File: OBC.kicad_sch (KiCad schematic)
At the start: 0 parts

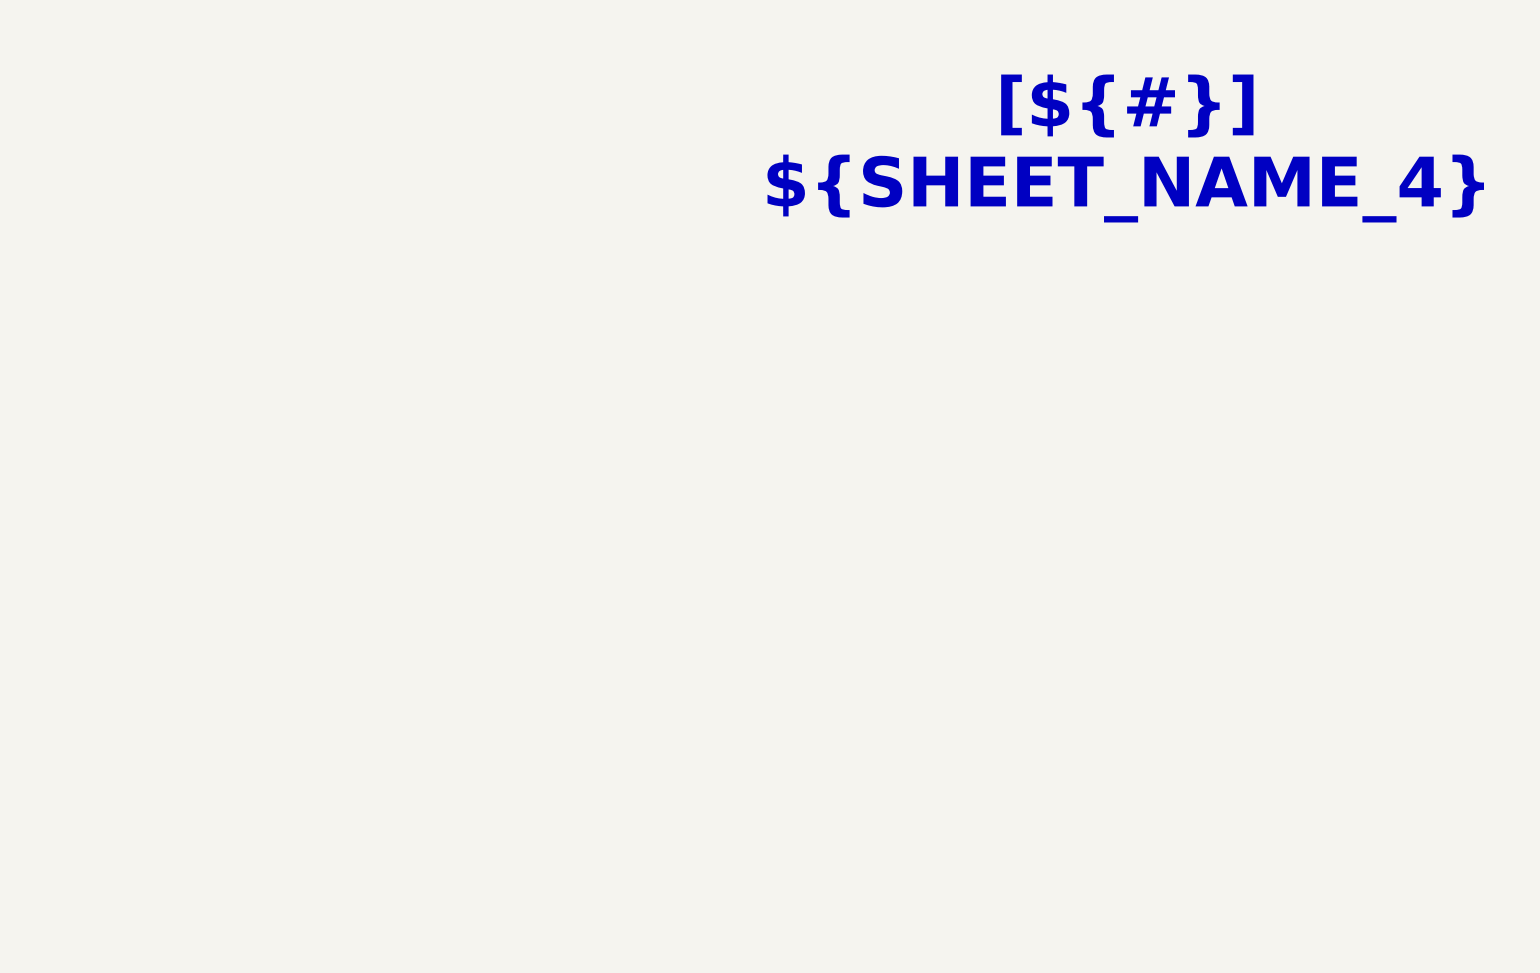
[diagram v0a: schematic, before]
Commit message: Pasted schematics from previous design
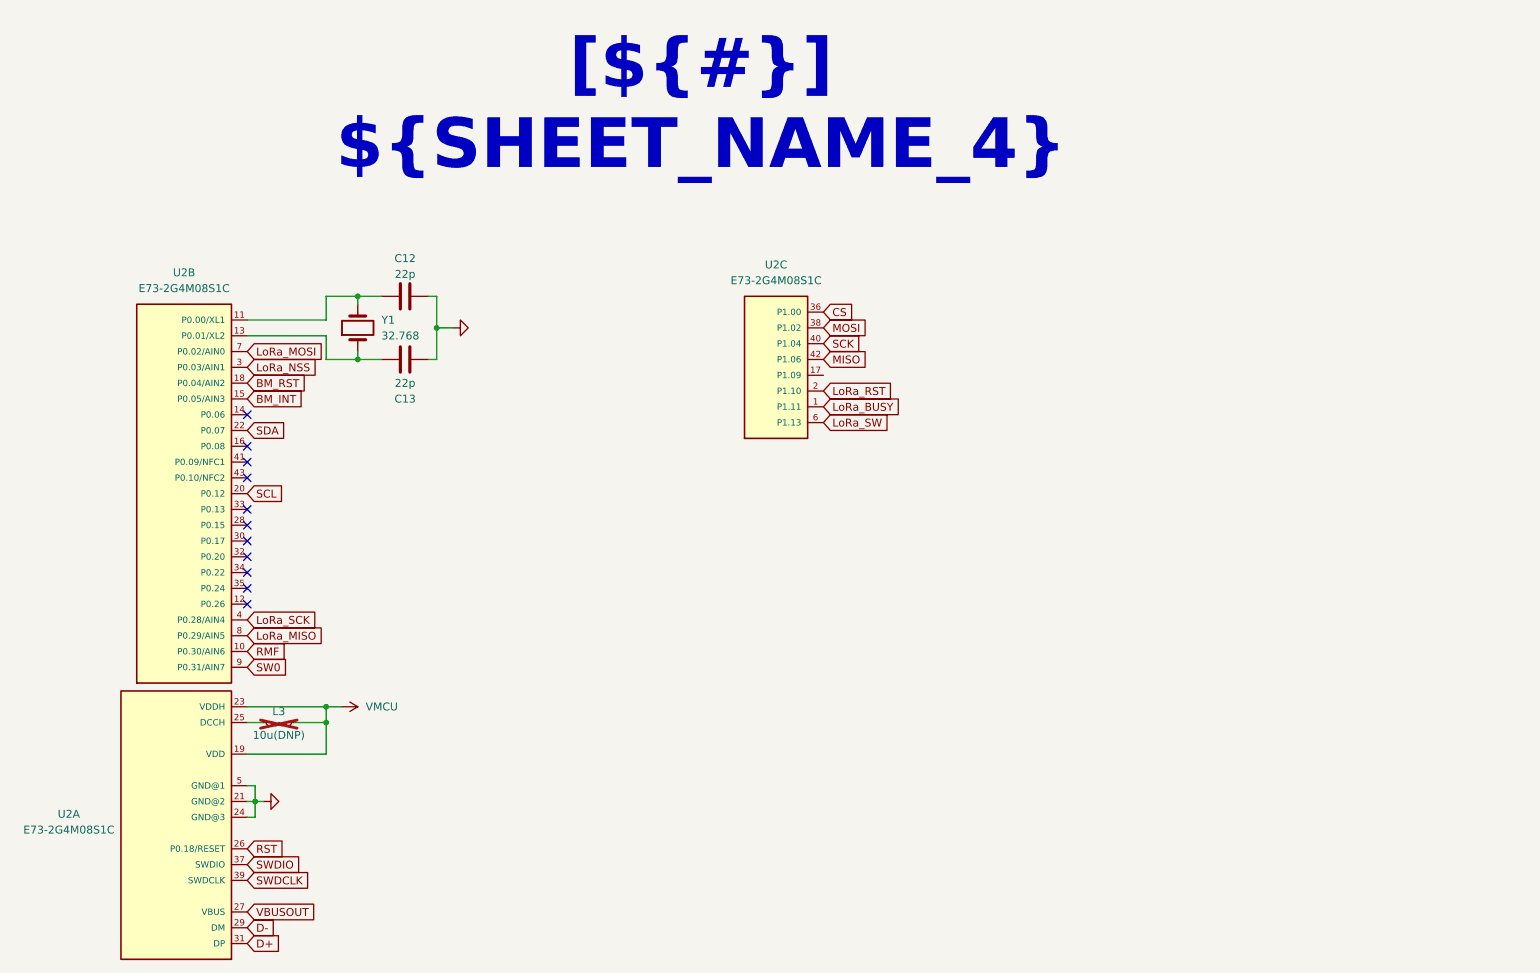
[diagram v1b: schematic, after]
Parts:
- added C12, C13: 22p, Capacitor_SMD:C_1206_3216Metric_Pad1.33x1.80mm_HandSolder, symbol Device:C
- added L3: 10u(DNP), Inductor_SMD:L_Changjiang_FTC201610D, symbol Device:L_Small
- added U2: E73-2G4M08S1C, Project_Components:E73-2G4M08S1C, symbol Project_Components:E73-2G4M08S1C
- added Y1: 32.768, Project_Components:WE-XTAL_CFPX-217, symbol Device:Crystal
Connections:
- new net: C12.2, U2.11 (P0.00/XL1), Y1.2
- new net: C13.2, U2.13 (P0.01/XL2), Y1.1
- new net: L3.1, U2.25 (DCCH)
- new net BM_INT: U2.15 (P0.05/AIN3)
- new net BM_RST: U2.18 (P0.04/AIN2)
- new net CS: U2.36 (P1.00)
- new net D+: U2.31 (DP)
- new net D-: U2.29 (DM)
- new net GND: C12.1, C13.1, U2.21 (GND@2), U2.24 (GND@3), U2.5 (GND@1)
- new net LoRa_BUSY: U2.1 (P1.11)
- new net LoRa_MISO: U2.8 (P0.29/AIN5)
- new net LoRa_MOSI: U2.7 (P0.02/AIN0)
- new net LoRa_NSS: U2.3 (P0.03/AIN1)
- new net LoRa_RST: U2.2 (P1.10)
- new net LoRa_SCK: U2.4 (P0.28/AIN4)
- new net LoRa_SW: U2.6 (P1.13)
- new net MISO: U2.42 (P1.06)
- new net MOSI: U2.38 (P1.02)
- new net RMF: U2.10 (P0.30/AIN6)
- new net RST: U2.26 (P0.18/RESET)
- new net SCK: U2.40 (P1.04)
- new net SCL: U2.20 (P0.12)
- new net SDA: U2.22 (P0.07)
- new net SW0: U2.9 (P0.31/AIN7)
- new net SWDCLK: U2.39 (SWDCLK)
- new net SWDIO: U2.37 (SWDIO)
- new net VBUSOUT: U2.27 (VBUS)
- new net VMCU: L3.2, U2.19 (VDD), U2.23 (VDDH)
- no-connect marks 0 -> 11

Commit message: Changed a few preferences
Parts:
- C12, C13: footprint Capacitor_SMD:C_1206_3216Metric_Pad1.33x1.80mm_HandSolder -> Capacitor_SMD:C_0603_1608Metric
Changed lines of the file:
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@@
 			)
 		)
-		(property "Footprint" "Capacitor_SMD:C_1206_3216Metric_Pad1.33x1.80mm_HandSolder"
+		(property "Footprint" "Capacitor_SMD:C_0603_1608Metric"
 			(at 90.17 67.6148 0)
 			(hide yes)
@@
 			)
 		)
-		(property "Footprint" "Capacitor_SMD:C_1206_3216Metric_Pad1.33x1.80mm_HandSolder"
+		(property "Footprint" "Capacitor_SMD:C_0603_1608Metric"
 			(at 90.17 59.3852 0)
 			(hide yes)

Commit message: Finished preliminary project schematics and architecture
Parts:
- U1: renamed from U2; footprint Project_Components:E73-2G4M08S1C -> E73-2G4M08S1C:E73-2G4M08S1C
- renumbered C12 to C1, C13 to C2, L3 to L1

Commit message: Edited ci.yaml
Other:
- moved on the sheet: C1, C2, Y1
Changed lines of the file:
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@@
-	)
-	(junction
-		(at 86.36 68.58)
-		(diameter 0)
-		(color 0 0 0 0)
 	)
 	(junction
@@
 	)
 	(junction
-		(at 99.06 63.5)
+		(at 88.9 68.58)
 		(diameter 0)
 		(color 0 0 0 0)
 	)
 	(junction
-		(at 86.36 58.42)
+		(at 101.6 63.5)
 		(diameter 0)
 		(color 0 0 0 0)
@@
 		(color 0 0 0 0)
 	)
+	(junction
+		(at 88.9 58.42)
+		(diameter 0)
+		(color 0 0 0 0)
+	)
 	(no_connect
 		(at 68.58 92.71)
@@
 	(wire
 		(pts
-			(xy 81.28 62.23) (xy 68.58 62.23)
+			(xy 82.55 62.23) (xy 68.58 62.23)
 		)
 		(stroke
@@
 	(wire
 		(pts
-			(xy 99.06 63.5) (xy 99.06 58.42)
-		)
-		(stroke
-			(width 0)
-			(type default)
-		)
-	)
-	(wire
-		(pts
-			(xy 81.28 68.58) (xy 81.28 64.77)
+			(xy 101.6 63.5) (xy 101.6 58.42)
+		)
+		(stroke
+			(width 0)
+			(type default)
+		)
+	)
+	(wire
+		(pts
+			(xy 82.55 68.58) (xy 82.55 64.77)
 		)
 		(stroke
@@
 	(wire
 		(pts
-			(xy 81.28 68.58) (xy 86.36 68.58)
-		)
-		(stroke
-			(width 0)
-			(type default)
-		)
-	)
-	(wire
-		(pts
-			(xy 86.36 58.42) (xy 86.36 59.69)
+			(xy 82.55 68.58) (xy 88.9 68.58)
+		)
+		(stroke
+			(width 0)
+			(type default)
+		)
+	)
+	(wire
+		(pts
+			(xy 88.9 58.42) (xy 88.9 59.69)
 		)
 		(stroke
@@
 	(wire
 		(pts
-			(xy 81.28 58.42) (xy 81.28 62.23)
-		)
-		(stroke
-			(width 0)
-			(type default)
-		)
-	)
-	(wire
-		(pts
-			(xy 101.6 63.5) (xy 99.06 63.5)
+			(xy 82.55 58.42) (xy 82.55 62.23)
+		)
+		(stroke
+			(width 0)
+			(type default)
+		)
+	)
+	(wire
+		(pts
+			(xy 104.14 63.5) (xy 101.6 63.5)
 		)
 		(stroke
@@
 	(wire
 		(pts
-			(xy 81.28 64.77) (xy 68.58 64.77)
+			(xy 82.55 64.77) (xy 68.58 64.77)
 		)
 		(stroke
@@
 	(wire
 		(pts
-			(xy 99.06 58.42) (xy 97.79 58.42)
+			(xy 101.6 58.42) (xy 100.33 58.42)
 		)
 		(stroke
@@
 	(wire
 		(pts
-			(xy 86.36 68.58) (xy 90.17 68.58)
+			(xy 88.9 68.58) (xy 92.71 68.58)
 		)
 		(stroke
@@
 	(wire
 		(pts
-			(xy 86.36 68.58) (xy 86.36 67.31)
+			(xy 88.9 68.58) (xy 88.9 67.31)
 		)
 		(stroke
@@
 	(wire
 		(pts
-			(xy 86.36 58.42) (xy 90.17 58.42)
+			(xy 88.9 58.42) (xy 92.71 58.42)
 		)
 		(stroke
@@
 	(wire
 		(pts
-			(xy 97.79 68.58) (xy 99.06 68.58)
+			(xy 100.33 68.58) (xy 101.6 68.58)
 		)
 		(stroke
@@
 	(wire
 		(pts
-			(xy 81.28 58.42) (xy 86.36 58.42)
+			(xy 82.55 58.42) (xy 88.9 58.42)
 		)
 		(stroke
@@
 	(wire
 		(pts
-			(xy 99.06 68.58) (xy 99.06 63.5)
+			(xy 101.6 68.58) (xy 101.6 63.5)
 		)
 		(stroke
@@
 	(symbol
 		(lib_id "power:GND")
-		(at 101.6 63.5 90)
+		(at 104.14 63.5 90)
 		(unit 1)
 		(body_style 1)
@@
 		(fields_autoplaced yes)
 		(property "Reference" "#PWR041"
-			(at 107.95 63.5 0)
+			(at 110.49 63.5 0)
 			(hide yes)
 			(show_name no)
@@
 		)
 		(property "Value" "GND"
-			(at 105.41 63.4999 90)
+			(at 107.95 63.4999 90)
 			(hide yes)
 			(show_name no)
@@
 		)
 		(property "Footprint" ""
-			(at 101.6 63.5 0)
+			(at 104.14 63.5 0)
 			(hide yes)
 			(show_name no)
@@
 		)
 		(property "Datasheet" ""
-			(at 101.6 63.5 0)
+			(at 104.14 63.5 0)
 			(hide yes)
 			(show_name no)
@@
 		)
 		(property "Description" "Power symbol creates a global label with name \"GND\" , ground"
-			(at 101.6 63.5 0)
+			(at 104.14 63.5 0)
 			(hide yes)
 			(show_name no)
@@
 	(symbol
 		(lib_id "Device:C")
-		(at 93.98 68.58 270)
+		(at 96.52 68.58 270)
 		(mirror x)
 		(unit 1)
@@
 		(dnp no)
 		(property "Reference" "C2"
-			(at 93.98 74.93 90)
+			(at 96.52 74.93 90)
 			(show_name no)
 			(do_not_autoplace no)
@@
 		)
 		(property "Value" "22p"
-			(at 93.98 72.39 90)
+			(at 96.52 72.39 90)
 			(show_name no)
 			(do_not_autoplace no)
@@
 		)
 		(property "Footprint" "Capacitor_SMD:C_0603_1608Metric"
-			(at 90.17 67.6148 0)
+			(at 92.71 67.6148 0)
 			(hide yes)
 			(show_name no)
@@
 		)
 		(property "Datasheet" ""
-			(at 93.98 68.58 0)
+			(at 96.52 68.58 0)
 			(hide yes)
 			(show_name no)
@@
 		)
 		(property "Description" "Unpolarized capacitor"
-			(at 93.98 68.58 0)
+			(at 96.52 68.58 0)
 			(hide yes)
 			(show_name no)
@@
 	(symbol
 		(lib_id "Device:Crystal")
-		(at 86.36 63.5 90)
+		(at 88.9 63.5 90)
 		(unit 1)
 		(body_style 1)
@@
 		(fields_autoplaced yes)
 		(property "Reference" "Y1"
-			(at 90.17 62.2299 90)
+			(at 92.71 62.2299 90)
 			(show_name no)
 			(do_not_autoplace no)
@@
 		)
 		(property "Value" "32.768"
-			(at 90.17 64.7699 90)
+			(at 92.71 64.7699 90)
 			(show_name no)
 			(do_not_autoplace no)
@@
 		)
 		(property "Footprint" "Project_Components:WE-XTAL_CFPX-217"
-			(at 86.36 63.5 0)
+			(at 88.9 63.5 0)
 			(hide yes)
 			(show_name no)
@@
 		)
 		(property "Datasheet" ""
-			(at 86.36 63.5 0)
+			(at 88.9 63.5 0)
 			(hide yes)
 			(show_name no)
@@
 		)
 		(property "Description" "Two pin crystal"
-			(at 86.36 63.5 0)
+			(at 88.9 63.5 0)
 			(hide yes)
 			(show_name no)
@@
 	(symbol
 		(lib_id "Device:C")
-		(at 93.98 58.42 270)
+		(at 96.52 58.42 270)
 		(unit 1)
 		(body_style 1)
@@
 		(dnp no)
 		(property "Reference" "C1"
-			(at 93.98 52.324 90)
+			(at 96.52 52.324 90)
 			(show_name no)
 			(do_not_autoplace no)
@@
 		)
 		(property "Value" "22p"
-			(at 93.98 54.864 90)
+			(at 96.52 54.864 90)
 			(show_name no)
 			(do_not_autoplace no)
@@
 		)
 		(property "Footprint" "Capacitor_SMD:C_0603_1608Metric"
-			(at 90.17 59.3852 0)
+			(at 92.71 59.3852 0)
 			(hide yes)
 			(show_name no)
@@
 		)
 		(property "Datasheet" ""
-			(at 93.98 58.42 0)
+			(at 96.52 58.42 0)
 			(hide yes)
 			(show_name no)
@@
 		)
 		(property "Description" "Unpolarized capacitor"
-			(at 93.98 58.42 0)
-			(hide yes)
-			(show_name no)
+			(at 96.52 58.42 0)
+			(hide yes)
+			(show_name no)

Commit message: Minor schematic adjustments
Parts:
- removed Y1: 32.768, Project_Components:WE-XTAL_CFPX-217, symbol Device:Crystal
- added Y1: 32.768, Project_Components:WE-XTAL_CFPX-217, symbol Project_Components:WE-XTAL_CFPX-217
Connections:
- net at C1.2, U1.11 (P0.00/XL1): now also Y1.2
- net at C2.2, U1.13 (P0.01/XL2): now also Y1.1
- no-connect marks 11 -> 12
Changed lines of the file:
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@@
+	)
+	(no_connect
+		(at 161.29 71.12)
 	)
 	(no_connect
@@
 	(wire
 		(pts
-			(xy 88.9 58.42) (xy 88.9 59.69)
+			(xy 88.9 58.42) (xy 88.9 60.96)
 		)
 		(stroke
@@
 	(wire
 		(pts
-			(xy 88.9 68.58) (xy 88.9 67.31)
+			(xy 88.9 66.04) (xy 88.9 68.58)
 		)
 		(stroke
@@
 	)
 	(symbol
-		(lib_id "Device:Crystal")
-		(at 88.9 63.5 90)
-		(unit 1)
-		(body_style 1)
-		(exclude_from_sim no)
-		(in_bom yes)
-		(on_board yes)
-		(in_pos_files yes)
-		(dnp no)
-		(fields_autoplaced yes)
-		(property "Reference" "Y1"
-			(at 92.71 62.2299 90)
-			(show_name no)
-			(do_not_autoplace no)
-			(effects
-				(font
-					(size 1.27 1.27)
-				)
-				(justify right)
-			)
-		)
-		(property "Value" "32.768"
-			(at 92.71 64.7699 90)
-			(show_name no)
-			(do_not_autoplace no)
-			(effects
-				(font
-					(size 1.27 1.27)
-				)
-				(justify right)
-			)
-		)
-		(property "Footprint" "Project_Components:WE-XTAL_CFPX-217"
-			(at 88.9 63.5 0)
-			(hide yes)
-			(show_name no)
-			(do_not_autoplace no)
-			(effects
-				(font
-					(size 1.27 1.27)
-				)
-			)
-		)
-		(property "Datasheet" ""
-			(at 88.9 63.5 0)
-			(hide yes)
-			(show_name no)
-			(do_not_autoplace no)
-			(effects
-				(font
-					(size 1.27 1.27)
-				)
-			)
-		)
-		(property "Description" "Two pin crystal"
-			(at 88.9 63.5 0)
-			(hide yes)
-			(show_name no)
-			(do_not_autoplace no)
-			(effects
-				(font
-					(size 1.27 1.27)
-				)
-			)
-		)
-		(pin "2"
-		)
-		(pin "1"
-		)
-		(instances
-			(project "CanSat_Devboard"
-				(path "/f9e05184-c88b-4a88-ae9c-ab2bdb32be7c/5d00bd0a-3bbf-46b2-b8c5-f75441fb4350/2028456c-6ef4-4d71-987d-d023cb9d3da5"
-					(reference "Y1")
-					(unit 1)
-				)
-			)
-		)
-	)
-	(symbol
 		(lib_id "Device:L_Small")
 		(at 73.66 127 90)
@@
 				)
 			)
+		)
+	)
+	(symbol
+		(lib_id "Project_Components:WE-XTAL_CFPX-217")
+		(at 88.9 63.5 90)
+		(unit 1)
+		(body_style 1)
+		(exclude_from_sim no)
+		(in_bom yes)
+		(on_board yes)
+		(in_pos_files yes)
+		(dnp no)
+		(property "Reference" "Y1"
+			(at 91.44 62.2299 90)
+			(show_name no)
+			(do_not_autoplace no)
+			(effects
+				(font
+					(size 1.27 1.27)
+				)
+				(justify right)
+			)
+		)
+		(property "Value" "32.768"
+			(at 91.186 64.77 90)
+			(show_name no)
+			(do_not_autoplace no)
+			(effects
+				(font
+					(size 1.27 1.27)
+				)
+				(justify right)
+			)
+		)
+		(property "Footprint" "Project_Components:WE-XTAL_CFPX-217"
+			(at 88.9 63.5 0)
+			(hide yes)
+			(show_name no)
+			(do_not_autoplace no)
+			(effects
+				(font
+					(size 1.27 1.27)
+				)
+			)
+		)
+		(property "Datasheet" ""
+			(at 88.9 63.5 0)
+			(hide yes)
+			(show_name no)
+			(do_not_autoplace no)
+			(effects
+				(font
+					(size 1.27 1.27)
+				)
+			)
+		)
+		(property "Description" "32.768 kHz ±20ppm Crystal 12.5pF 70 kOhms 2-SMD, No Lead"
+			(at 88.9 63.5 0)
+			(hide yes)
+			(show_name no)
+			(do_not_autoplace no)
+			(effects
+				(font
+					(size 1.27 1.27)
+				)
+				(justify bottom)
+			)
+		)
+		(property "MF" "Würth Elektronik"
+			(at 88.9 63.5 0)
+			(hide yes)
+			(show_name no)
+			(do_not_autoplace no)
+			(effects
+				(font
+					(size 1.27 1.27)
+				)
+				(justify bottom)
+			)
+		)
+		(property "Package" "None"
+			(at 88.9 63.5 0)
+			(hide yes)
+			(show_name no)
+			(do_not_autoplace no)
+			(effects
+				(font
+					(size 1.27 1.27)
+				)
+				(justify bottom)
+			)
+		)
+		(property "Price" "None"
+			(at 88.9 63.5 0)
+			(hide yes)
+			(show_name no)
+			(do_not_autoplace no)
+			(effects
+				(font
+					(size 1.27 1.27)
+				)
+				(justify bottom)
+			)
+		)
+		(property "SnapEDA_Link" "https://www.snapeda.com/parts/830009678/W%25C3%25BCrth+Elektronik+Midcom/view-part/?ref=snap"
+			(at 88.9 63.5 0)
+			(hide yes)
+			(show_name no)
+			(do_not_autoplace no)
+			(effects
+				(font
+					(size 1.27 1.27)
+				)
+				(justify bottom)
+			)
+		)
+		(property "MP" "830009678"
+			(at 88.9 63.5 0)
+			(hide yes)
+			(show_name no)
+			(do_not_autoplace no)
+			(effects
+				(font
+					(size 1.27 1.27)
+				)
+				(justify bottom)
+			)
+		)
+		(property "Availability" "In Stock"
+			(at 88.9 63.5 0)
+			(hide yes)
+			(show_name no)
+			(do_not_autoplace no)
+			(effects
+				(font
+					(size 1.27 1.27)
+				)
+				(justify bottom)
+			)
+		)
+		(property "Check_prices" "https://www.snapeda.com/parts/830009678/W%25C3%25BCrth+Elektronik+Midcom/view-part/?ref=eda"
+			(at 88.9 63.5 0)
+			(hide yes)
+			(show_name no)
+			(do_not_autoplace no)
+			(effects
+				(font
+					(size 1.27 1.27)
+				)
+				(justify bottom)
+			)
+		)
+		(pin "2"
+		)
+		(pin "1"
+		)
+		(instances
+			(project "CanSat_Devboard"
+				(path "/f9e05184-c88b-4a88-ae9c-ab2bdb32be7c/5d00bd0a-3bbf-46b2-b8c5-f75441fb4350/2028456c-6ef4-4d71-987d-d023cb9d3da5"
+					(reference "Y1")
+					(unit 1)
+				)
+			)
